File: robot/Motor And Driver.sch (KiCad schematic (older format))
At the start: 1 part

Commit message: Motor driver
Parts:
- removed U?: A4988SETTR-T, digikey-footprints:VFQFN-28-1EP_5x5mm, symbol dk_PMIC-Motor-Drivers-Controllers:A4988SETTR-T
- added C? (x2): 2.2µ, symbol Device:C
- added C? (x2): 0.01µ, symbol Device:C
- added C? (x2): 10µ, symbol Device:C
- added M? (x2): Stepper_Motor_bipolar, symbol Motor:Stepper_Motor_bipolar
- added R? (x4): 0.8, symbol Device:R
- added U? (x2): DRV8833PWP, Package_SO:HTSSOP-16-1EP_4.4x5mm_P0.65mm_EP3.4x5mm_Mask2.46x2.31mm_ThermalVias, symbol Driver_Motor:DRV8833PWP
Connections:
- net labels added: +3V3, GND, M1_AIN1, M1_AIN2, M1_BIN1, M1_BIN2, M1_SLEEP, M2_AIN1, M2_AIN2, M2_BIN1, M2_BIN2, M2_SLEEP
- wire segments 0 -> 86
- no-connect marks 0 -> 2

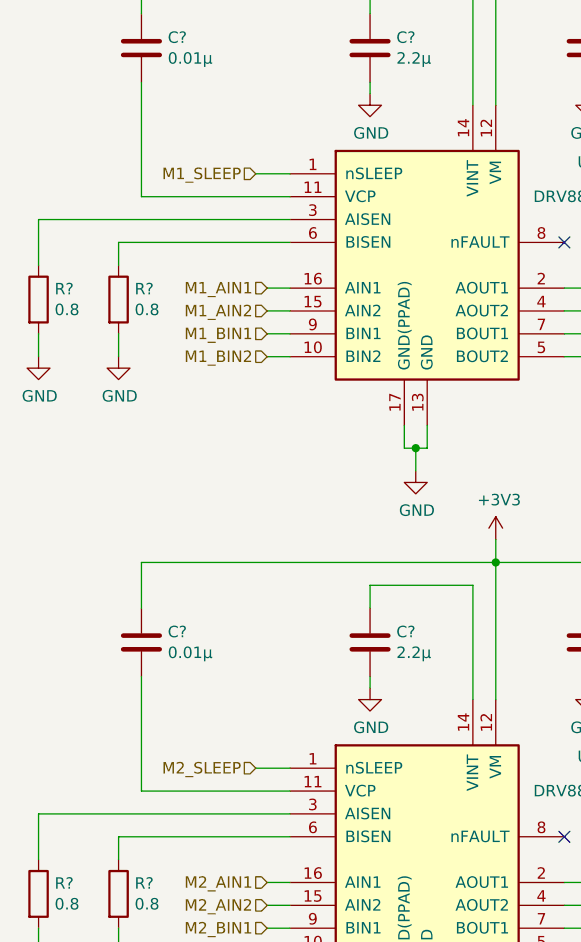
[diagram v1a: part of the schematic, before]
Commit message: UI parts, (re)wiring remaining signals
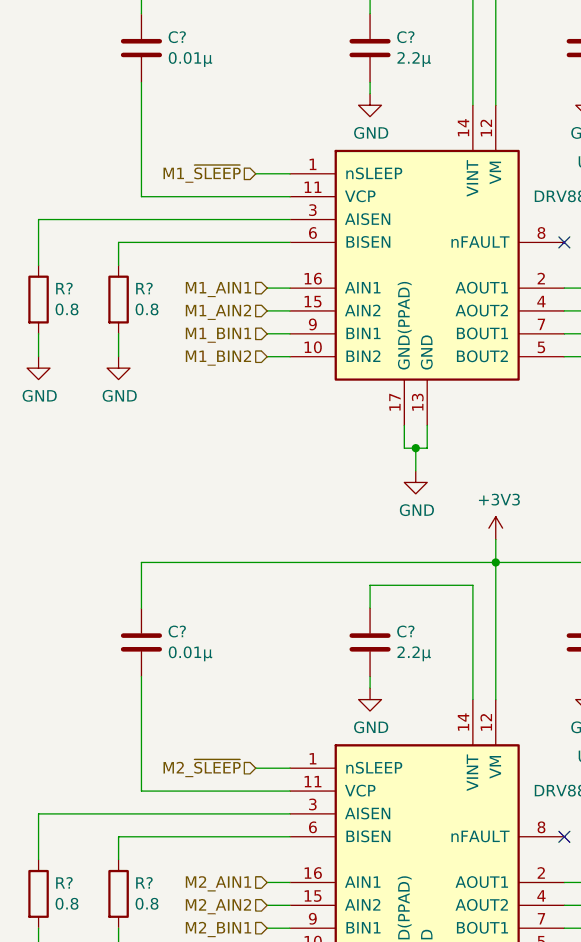
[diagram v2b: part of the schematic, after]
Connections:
- net M1_SLEEP renamed M1_~SLEEP
- net M2_SLEEP renamed M2_~SLEEP
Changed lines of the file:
@@
 $Descr A4 11693 8268
 encoding utf-8
-Sheet 7 7
+Sheet 6 8
 Title ""
 Date ""
@@
 	4850 2750 4950 2750
 Text HLabel 4800 2250 0    50   Input ~ 0
-M1_SLEEP
+M1_~SLEEP
 Wire Wire Line
 	4800 2250 4950 2250
@@
 	4850 5350 4950 5350
 Text HLabel 4800 4850 0    50   Input ~ 0
-M2_SLEEP
+M2_~SLEEP
 Wire Wire Line
 	4800 4850 4950 4850

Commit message: DRC check fixes and small changes
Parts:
- gave numbers to parts that had none: 14
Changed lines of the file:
@@
 $EndDescr
 $Comp
-L Driver_Motor:DRV8833PWP U?
+L Driver_Motor:DRV8833PWP U7
 U 1 1 5D6819C7
 P 5550 2650
-F 0 "U?" H 6250 3100 50  0000 C CNN
+F 0 "U7" H 6250 3100 50  0000 C CNN
 F 1 "DRV8833PWP" H 6250 2950 50  0000 C CNN
 F 2 "Package_SO:HTSSOP-16-1EP_4.4x5mm_P0.65mm_EP3.4x5mm_Mask2.46x2.31mm_ThermalVias" H 6000 3100 50  0001 L CNN
@@
 $EndComp
 $Comp
-L power:GND #PWR?
+L power:GND #PWR08
 U 1 1 5D6829B3
 P 5500 3550
-F 0 "#PWR?" H 5500 3300 50  0001 C CNN
+F 0 "#PWR08" H 5500 3300 50  0001 C CNN
 F 1 "GND" H 5505 3377 50  0000 C CNN
 F 2 "" H 5500 3550 50  0001 C CNN
@@
 Connection ~ 5500 3450
 $Comp
-L Motor:Stepper_Motor_bipolar M?
+L Motor:Stepper_Motor_bipolar M1
 U 1 1 5D673CFA
 P 7650 2800
-F 0 "M?" H 7838 2924 50  0000 L CNN
+F 0 "M1" H 7838 2924 50  0000 L CNN
 F 1 "Stepper_Motor_bipolar" H 7838 2833 50  0000 L CNN
 F 2 "" H 7660 2790 50  0001 C CNN
@@
 	7250 3050 6150 3050
 $Comp
-L Device:C C?
+L Device:C C9
 U 1 1 5D684384
 P 5300 1700
-F 0 "C?" H 5415 1746 50  0000 L CNN
+F 0 "C9" H 5415 1746 50  0000 L CNN
 F 1 "2.2µ" H 5415 1655 50  0000 L CNN
 F 2 "" H 5338 1550 50  0001 C CNN
@@
 $EndComp
 $Comp
-L power:GND #PWR?
+L power:GND #PWR04
 U 1 1 5D68634E
 P 5300 1900
-F 0 "#PWR?" H 5300 1650 50  0001 C CNN
+F 0 "#PWR04" H 5300 1650 50  0001 C CNN
 F 1 "GND" H 5305 1727 50  0000 C CNN
 F 2 "" H 5300 1900 50  0001 C CNN
@@
 	5300 1850 5300 1900
 $Comp
-L Device:C C?
+L Device:C C8
 U 1 1 5D6907BC
 P 4300 1700
-F 0 "C?" H 4415 1746 50  0000 L CNN
+F 0 "C8" H 4415 1746 50  0000 L CNN
 F 1 "0.01µ" H 4415 1655 50  0000 L CNN
 F 2 "" H 4338 1550 50  0001 C CNN
@@
 	4300 2350 4950 2350
 $Comp
-L Device:C C?
+L Device:C C10
 U 1 1 5D694F60
 P 6250 1700
-F 0 "C?" H 6365 1746 50  0000 L CNN
+F 0 "C10" H 6365 1746 50  0000 L CNN
 F 1 "10µ" H 6365 1655 50  0000 L CNN
 F 2 "" H 6288 1550 50  0001 C CNN
@@
 	6250 1850 6250 1900
 $Comp
-L power:GND #PWR?
+L power:GND #PWR05
 U 1 1 5D6965F5
 P 6250 1900
-F 0 "#PWR?" H 6250 1650 50  0001 C CNN
+F 0 "#PWR05" H 6250 1650 50  0001 C CNN
 F 1 "GND" H 6255 1727 50  0000 C CNN
 F 2 "" H 6250 1900 50  0001 C CNN
@@
 	5850 1350 5850 1250
 $Comp
-L power:+3V3 #PWR?
+L power:+3V3 #PWR03
 U 1 1 5D69785B
 P 5850 1250
-F 0 "#PWR?" H 5850 1100 50  0001 C CNN
+F 0 "#PWR03" H 5850 1100 50  0001 C CNN
 F 1 "+3V3" H 5865 1423 50  0000 C CNN
 F 2 "" H 5850 1250 50  0001 C CNN
@@
 NoConn ~ 6150 2550
 $Comp
-L Device:R R?
+L Device:R R11
 U 1 1 5D699455
 P 3850 2800
-F 0 "R?" H 3920 2846 50  0000 L CNN
+F 0 "R11" H 3920 2846 50  0000 L CNN
 F 1 "0.8" H 3920 2755 50  0000 L CNN
 F 2 "" V 3780 2800 50  0001 C CNN
@@
 $EndComp
 $Comp
-L Device:R R?
+L Device:R R12
 U 1 1 5D699C1A
 P 4200 2800
-F 0 "R?" H 4270 2846 50  0000 L CNN
+F 0 "R12" H 4270 2846 50  0000 L CNN
 F 1 "0.8" H 4270 2755 50  0000 L CNN
 F 2 "" V 4130 2800 50  0001 C CNN
@@
 $EndComp
 $Comp
-L power:GND #PWR?
+L power:GND #PWR06
 U 1 1 5D699FF9
 P 3850 3050
-F 0 "#PWR?" H 3850 2800 50  0001 C CNN
+F 0 "#PWR06" H 3850 2800 50  0001 C CNN
 F 1 "GND" H 3855 2877 50  0000 C CNN
 F 2 "" H 3850 3050 50  0001 C CNN
@@
 $EndComp
 $Comp
-L power:GND #PWR?
+L power:GND #PWR07
 U 1 1 5D69A37B
 P 4200 3050
-F 0 "#PWR?" H 4200 2800 50  0001 C CNN
+F 0 "#PWR07" H 4200 2800 50  0001 C CNN
 F 1 "GND" H 4205 2877 50  0000 C CNN
 F 2 "" H 4200 3050 50  0001 C CNN
@@
 	4800 2250 4950 2250
 $Comp
-L Driver_Motor:DRV8833PWP U?
+L Driver_Motor:DRV8833PWP U8
 U 1 1 5D6ABDA4
 P 5550 5250
-F 0 "U?" H 6250 5700 50  0000 C CNN
+F 0 "U8" H 6250 5700 50  0000 C CNN
 F 1 "DRV8833PWP" H 6250 5550 50  0000 C CNN
 F 2 "Package_SO:HTSSOP-16-1EP_4.4x5mm_P0.65mm_EP3.4x5mm_Mask2.46x2.31mm_ThermalVias" H 6000 5700 50  0001 L CNN
@@
 $EndComp
 $Comp
-L power:GND #PWR?
+L power:GND #PWR014
 U 1 1 5D6ABDAE
 P 5500 6150
-F 0 "#PWR?" H 5500 5900 50  0001 C CNN
+F 0 "#PWR014" H 5500 5900 50  0001 C CNN
 F 1 "GND" H 5505 5977 50  0000 C CNN
 F 2 "" H 5500 6150 50  0001 C CNN
@@
 Connection ~ 5500 6050
 $Comp
-L Motor:Stepper_Motor_bipolar M?
+L Motor:Stepper_Motor_bipolar M2
 U 1 1 5D6ABDBE
 P 7650 5400
-F 0 "M?" H 7838 5524 50  0000 L CNN
+F 0 "M2" H 7838 5524 50  0000 L CNN
 F 1 "Stepper_Motor_bipolar" H 7838 5433 50  0000 L CNN
 F 2 "" H 7660 5390 50  0001 C CNN
@@
 	7250 5650 6150 5650
 $Comp
-L Device:C C?
+L Device:C C12
 U 1 1 5D6ABDD6
 P 5300 4300
-F 0 "C?" H 5415 4346 50  0000 L CNN
+F 0 "C12" H 5415 4346 50  0000 L CNN
 F 1 "2.2µ" H 5415 4255 50  0000 L CNN
 F 2 "" H 5338 4150 50  0001 C CNN
@@
 $EndComp
 $Comp
-L power:GND #PWR?
+L power:GND #PWR010
 U 1 1 5D6ABDE0
 P 5300 4500
-F 0 "#PWR?" H 5300 4250 50  0001 C CNN
+F 0 "#PWR010" H 5300 4250 50  0001 C CNN
 F 1 "GND" H 5305 4327 50  0000 C CNN
 F 2 "" H 5300 4500 50  0001 C CNN
@@
 	5300 4450 5300 4500
 $Comp
-L Device:C C?
+L Device:C C11
 U 1 1 5D6ABDEE
 P 4300 4300
-F 0 "C?" H 4415 4346 50  0000 L CNN
+F 0 "C11" H 4415 4346 50  0000 L CNN
 F 1 "0.01µ" H 4415 4255 50  0000 L CNN
 F 2 "" H 4338 4150 50  0001 C CNN
@@
 	4300 4950 4950 4950
 $Comp
-L Device:C C?
+L Device:C C13
 U 1 1 5D6ABDFC
 P 6250 4300
-F 0 "C?" H 6365 4346 50  0000 L CNN
+F 0 "C13" H 6365 4346 50  0000 L CNN
 F 1 "10µ" H 6365 4255 50  0000 L CNN
 F 2 "" H 6288 4150 50  0001 C CNN
@@
 	6250 4450 6250 4500
 $Comp
-L power:GND #PWR?
+L power:GND #PWR011
 U 1 1 5D6ABE07
 P 6250 4500
-F 0 "#PWR?" H 6250 4250 50  0001 C CNN
+F 0 "#PWR011" H 6250 4250 50  0001 C CNN
 F 1 "GND" H 6255 4327 50  0000 C CNN
 F 2 "" H 6250 4500 50  0001 C CNN
@@
 	5850 3950 5850 3850
 $Comp
-L power:+3V3 #PWR?
+L power:+3V3 #PWR09
 U 1 1 5D6ABE16
 P 5850 3850
-F 0 "#PWR?" H 5850 3700 50  0001 C CNN
+F 0 "#PWR09" H 5850 3700 50  0001 C CNN
 F 1 "+3V3" H 5865 4023 50  0000 C CNN
 F 2 "" H 5850 3850 50  0001 C CNN
@@
 NoConn ~ 6150 5150
 $Comp
-L Device:R R?
+L Device:R R13
 U 1 1 5D6ABE21
 P 3850 5400
-F 0 "R?" H 3920 5446 50  0000 L CNN
+F 0 "R13" H 3920 5446 50  0000 L CNN
 F 1 "0.8" H 3920 5355 50  0000 L CNN
 F 2 "" V 3780 5400 50  0001 C CNN
@@
 $EndComp
 $Comp
-L Device:R R?
+L Device:R R14
 U 1 1 5D6ABE2B
 P 4200 5400
-F 0 "R?" H 4270 5446 50  0000 L CNN
+F 0 "R14" H 4270 5446 50  0000 L CNN
 F 1 "0.8" H 4270 5355 50  0000 L CNN
 F 2 "" V 4130 5400 50  0001 C CNN
@@
 $EndComp
 $Comp
-L power:GND #PWR?
+L power:GND #PWR012
 U 1 1 5D6ABE35
 P 3850 5650
-F 0 "#PWR?" H 3850 5400 50  0001 C CNN
+F 0 "#PWR012" H 3850 5400 50  0001 C CNN
 F 1 "GND" H 3855 5477 50  0000 C CNN
 F 2 "" H 3850 5650 50  0001 C CNN
@@
 $EndComp
 $Comp
-L power:GND #PWR?
+L power:GND #PWR013
 U 1 1 5D6ABE3F
 P 4200 5650
-F 0 "#PWR?" H 4200 5400 50  0001 C CNN
+F 0 "#PWR013" H 4200 5400 50  0001 C CNN
 F 1 "GND" H 4205 5477 50  0000 C CNN
 F 2 "" H 4200 5650 50  0001 C CNN

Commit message: Testpoints, switch, small changes
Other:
- moved on the sheet: C12, C9
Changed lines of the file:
@@
 U 1 1 5D6819C7
 P 5550 2650
-F 0 "U7" H 6250 3100 50  0000 C CNN
-F 1 "DRV8833PWP" H 6250 2950 50  0000 C CNN
+F 0 "U7" H 5200 3200 50  0000 C CNN
+F 1 "DRV8833PWP" H 5850 2100 50  0000 C CNN
 F 2 "Package_SO:HTSSOP-16-1EP_4.4x5mm_P0.65mm_EP3.4x5mm_Mask2.46x2.31mm_ThermalVias" H 6000 3100 50  0001 L CNN
 F 3 "http://www.ti.com/lit/ds/symlink/drv8833.pdf" H 5400 3200 50  0001 C CNN
@@
 $EndComp
 $Comp
-L power:GND #PWR08
+L power:GND #PWR035
 U 1 1 5D6829B3
 P 5500 3550
-F 0 "#PWR08" H 5500 3300 50  0001 C CNN
+F 0 "#PWR035" H 5500 3300 50  0001 C CNN
 F 1 "GND" H 5505 3377 50  0000 C CNN
 F 2 "" H 5500 3550 50  0001 C CNN
@@
 L Device:C C9
 U 1 1 5D684384
-P 5300 1700
-F 0 "C9" H 5415 1746 50  0000 L CNN
-F 1 "2.2µ" H 5415 1655 50  0000 L CNN
-F 2 "" H 5338 1550 50  0001 C CNN
-F 3 "~" H 5300 1700 50  0001 C CNN
-	1    5300 1700
-	1    0    0    -1
-$EndComp
-$Comp
-L power:GND #PWR04
+P 5450 1700
+F 0 "C9" H 5565 1746 50  0000 L CNN
+F 1 "2.2µ" H 5565 1655 50  0000 L CNN
+F 2 "" H 5488 1550 50  0001 C CNN
+F 3 "~" H 5450 1700 50  0001 C CNN
+	1    5450 1700
+	1    0    0    -1
+$EndComp
+$Comp
+L power:GND #PWR031
 U 1 1 5D68634E
-P 5300 1900
-F 0 "#PWR04" H 5300 1650 50  0001 C CNN
-F 1 "GND" H 5305 1727 50  0000 C CNN
-F 2 "" H 5300 1900 50  0001 C CNN
-F 3 "" H 5300 1900 50  0001 C CNN
-	1    5300 1900
+P 5450 1900
+F 0 "#PWR031" H 5450 1650 50  0001 C CNN
+F 1 "GND" H 5455 1727 50  0000 C CNN
+F 2 "" H 5450 1900 50  0001 C CNN
+F 3 "" H 5450 1900 50  0001 C CNN
+	1    5450 1900
 	1    0    0    -1
 $EndComp
@@
 	5750 1950 5750 1450
 Wire Wire Line
-	5750 1450 5300 1450
-Wire Wire Line
-	5300 1450 5300 1550
-Wire Wire Line
-	5300 1850 5300 1900
+	5750 1450 5450 1450
+Wire Wire Line
+	5450 1450 5450 1550
+Wire Wire Line
+	5450 1850 5450 1900
 $Comp
 L Device:C C8
@@
 	6250 1850 6250 1900
 $Comp
-L power:GND #PWR05
+L power:GND #PWR032
 U 1 1 5D6965F5
 P 6250 1900
-F 0 "#PWR05" H 6250 1650 50  0001 C CNN
+F 0 "#PWR032" H 6250 1650 50  0001 C CNN
 F 1 "GND" H 6255 1727 50  0000 C CNN
 F 2 "" H 6250 1900 50  0001 C CNN
@@
 	5850 1350 5850 1250
 $Comp
-L power:+3V3 #PWR03
+L power:+3V3 #PWR030
 U 1 1 5D69785B
 P 5850 1250
-F 0 "#PWR03" H 5850 1100 50  0001 C CNN
+F 0 "#PWR030" H 5850 1100 50  0001 C CNN
 F 1 "+3V3" H 5865 1423 50  0000 C CNN
 F 2 "" H 5850 1250 50  0001 C CNN
@@
 $EndComp
 $Comp
-L power:GND #PWR06
+L power:GND #PWR033
 U 1 1 5D699FF9
 P 3850 3050
-F 0 "#PWR06" H 3850 2800 50  0001 C CNN
+F 0 "#PWR033" H 3850 2800 50  0001 C CNN
 F 1 "GND" H 3855 2877 50  0000 C CNN
 F 2 "" H 3850 3050 50  0001 C CNN
@@
 $EndComp
 $Comp
-L power:GND #PWR07
+L power:GND #PWR034
 U 1 1 5D69A37B
 P 4200 3050
-F 0 "#PWR07" H 4200 2800 50  0001 C CNN
+F 0 "#PWR034" H 4200 2800 50  0001 C CNN
 F 1 "GND" H 4205 2877 50  0000 C CNN
 F 2 "" H 4200 3050 50  0001 C CNN
@@
 U 1 1 5D6ABDA4
 P 5550 5250
-F 0 "U8" H 6250 5700 50  0000 C CNN
-F 1 "DRV8833PWP" H 6250 5550 50  0000 C CNN
+F 0 "U8" H 5200 5800 50  0000 C CNN
+F 1 "DRV8833PWP" H 5850 4700 50  0000 C CNN
 F 2 "Package_SO:HTSSOP-16-1EP_4.4x5mm_P0.65mm_EP3.4x5mm_Mask2.46x2.31mm_ThermalVias" H 6000 5700 50  0001 L CNN
 F 3 "http://www.ti.com/lit/ds/symlink/drv8833.pdf" H 5400 5800 50  0001 C CNN
@@
 $EndComp
 $Comp
-L power:GND #PWR014
+L power:GND #PWR041
 U 1 1 5D6ABDAE
 P 5500 6150
-F 0 "#PWR014" H 5500 5900 50  0001 C CNN
+F 0 "#PWR041" H 5500 5900 50  0001 C CNN
 F 1 "GND" H 5505 5977 50  0000 C CNN
 F 2 "" H 5500 6150 50  0001 C CNN
@@
 L Device:C C12
 U 1 1 5D6ABDD6
-P 5300 4300
-F 0 "C12" H 5415 4346 50  0000 L CNN
-F 1 "2.2µ" H 5415 4255 50  0000 L CNN
-F 2 "" H 5338 4150 50  0001 C CNN
-F 3 "~" H 5300 4300 50  0001 C CNN
-	1    5300 4300
-	1    0    0    -1
-$EndComp
-$Comp
-L power:GND #PWR010
+P 5450 4300
+F 0 "C12" H 5565 4346 50  0000 L CNN
+F 1 "2.2µ" H 5565 4255 50  0000 L CNN
+F 2 "" H 5488 4150 50  0001 C CNN
+F 3 "~" H 5450 4300 50  0001 C CNN
+	1    5450 4300
+	1    0    0    -1
+$EndComp
+$Comp
+L power:GND #PWR037
 U 1 1 5D6ABDE0
-P 5300 4500
-F 0 "#PWR010" H 5300 4250 50  0001 C CNN
-F 1 "GND" H 5305 4327 50  0000 C CNN
-F 2 "" H 5300 4500 50  0001 C CNN
-F 3 "" H 5300 4500 50  0001 C CNN
-	1    5300 4500
+P 5450 4500
+F 0 "#PWR037" H 5450 4250 50  0001 C CNN
+F 1 "GND" H 5455 4327 50  0000 C CNN
+F 2 "" H 5450 4500 50  0001 C CNN
+F 3 "" H 5450 4500 50  0001 C CNN
+	1    5450 4500
 	1    0    0    -1
 $EndComp
@@
 	5750 4550 5750 4050
 Wire Wire Line
-	5750 4050 5300 4050
-Wire Wire Line
-	5300 4050 5300 4150
-Wire Wire Line
-	5300 4450 5300 4500
+	5750 4050 5450 4050
+Wire Wire Line
+	5450 4050 5450 4150
+Wire Wire Line
+	5450 4450 5450 4500
 $Comp
 L Device:C C11
@@
 	6250 4450 6250 4500
 $Comp
-L power:GND #PWR011
+L power:GND #PWR038
 U 1 1 5D6ABE07
 P 6250 4500
-F 0 "#PWR011" H 6250 4250 50  0001 C CNN
+F 0 "#PWR038" H 6250 4250 50  0001 C CNN
 F 1 "GND" H 6255 4327 50  0000 C CNN
 F 2 "" H 6250 4500 50  0001 C CNN
@@
 	5850 3950 5850 3850
 $Comp
-L power:+3V3 #PWR09
+L power:+3V3 #PWR036
 U 1 1 5D6ABE16
 P 5850 3850
-F 0 "#PWR09" H 5850 3700 50  0001 C CNN
+F 0 "#PWR036" H 5850 3700 50  0001 C CNN
 F 1 "+3V3" H 5865 4023 50  0000 C CNN
 F 2 "" H 5850 3850 50  0001 C CNN
@@
 $EndComp
 $Comp
-L power:GND #PWR012
+L power:GND #PWR039
 U 1 1 5D6ABE35
 P 3850 5650
-F 0 "#PWR012" H 3850 5400 50  0001 C CNN
+F 0 "#PWR039" H 3850 5400 50  0001 C CNN
 F 1 "GND" H 3855 5477 50  0000 C CNN
 F 2 "" H 3850 5650 50  0001 C CNN
@@
 $EndComp
 $Comp
-L power:GND #PWR013
+L power:GND #PWR040
 U 1 1 5D6ABE3F
 P 4200 5650
-F 0 "#PWR013" H 4200 5400 50  0001 C CNN
+F 0 "#PWR040" H 4200 5400 50  0001 C CNN
 F 1 "GND" H 4205 5477 50  0000 C CNN
 F 2 "" H 4200 5650 50  0001 C CNN
